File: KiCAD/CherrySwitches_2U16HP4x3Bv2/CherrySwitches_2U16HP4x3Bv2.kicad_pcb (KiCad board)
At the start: 2 copper layers, 80.9 x 84 mm, 16 parts

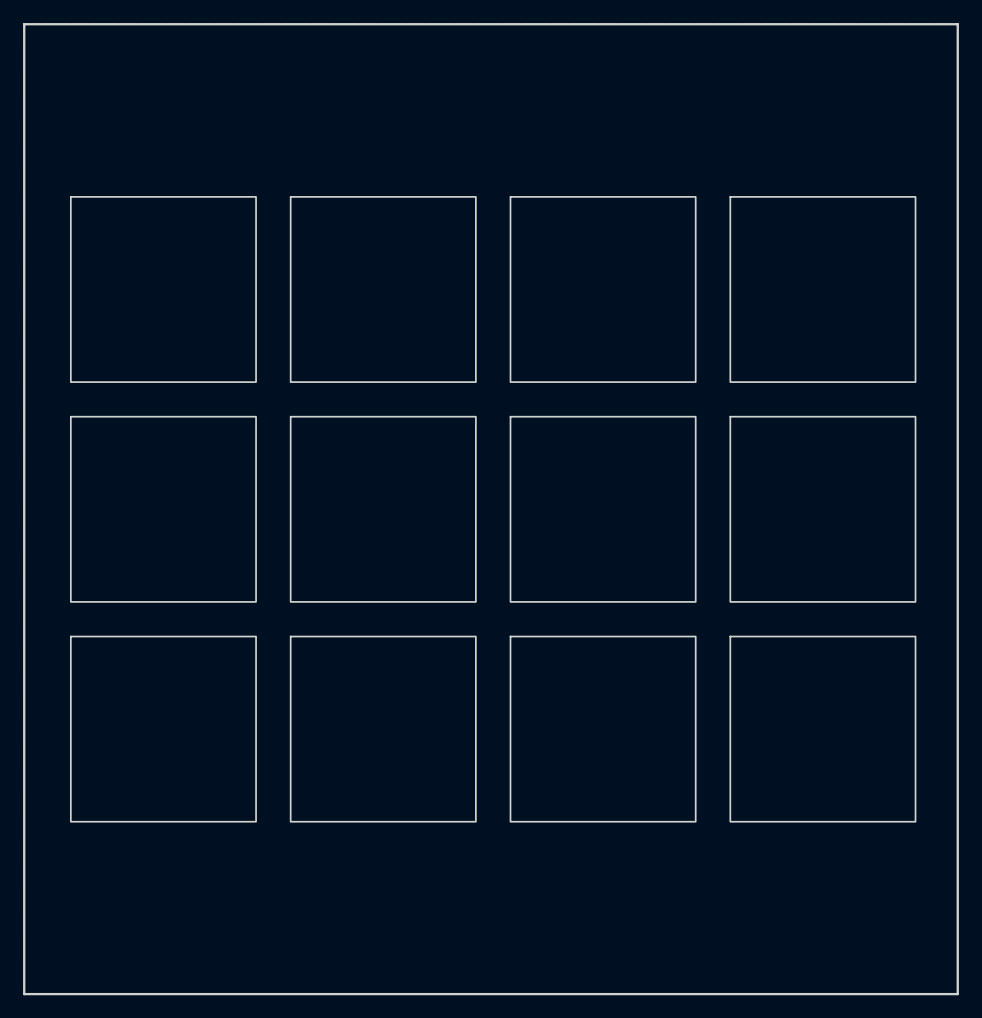
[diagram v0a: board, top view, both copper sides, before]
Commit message: updated all modules to use plated through-holes wherever possible
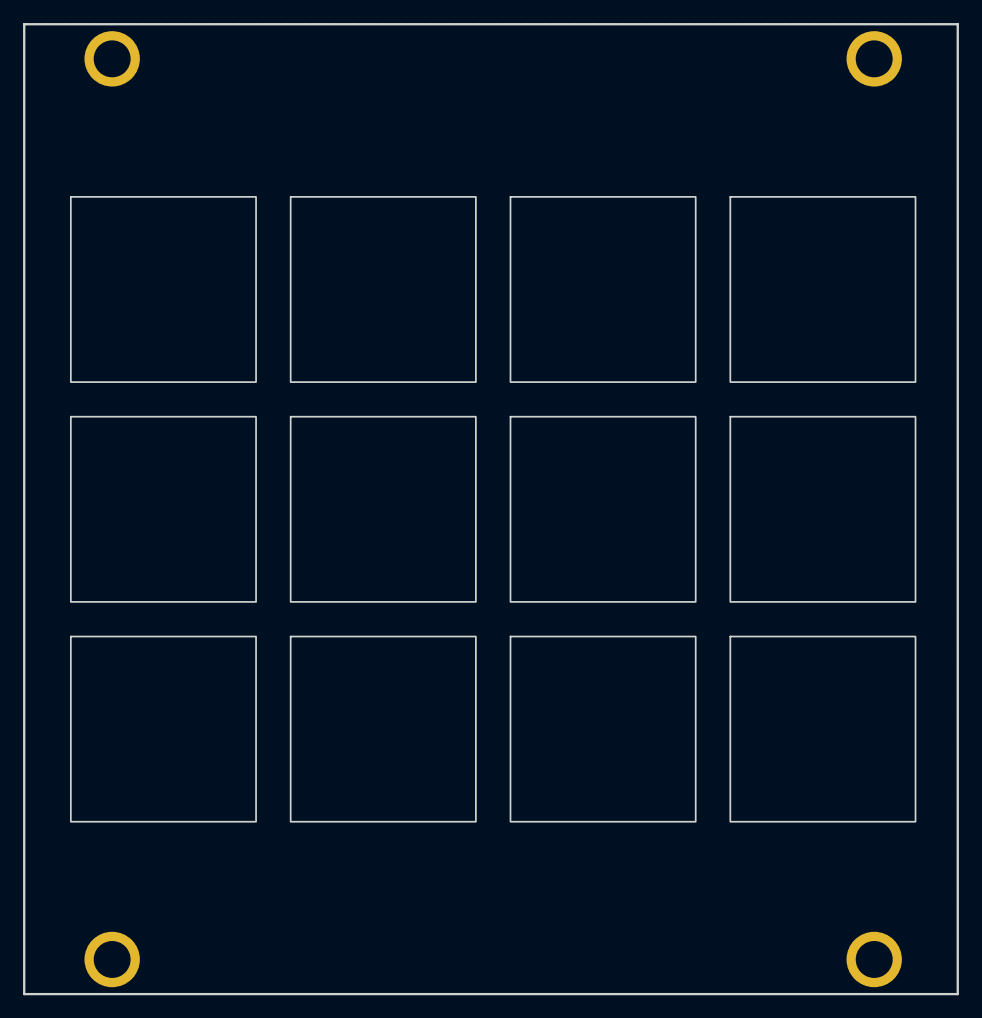
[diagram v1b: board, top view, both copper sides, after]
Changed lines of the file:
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@@
 			)
 		)
-		(pad "" np_thru_hole oval
+		(pad "" thru_hole circle
 			(at 0 0)
-			(size 4.34 3.2)
-			(drill oval 4.34 3.2)
+			(size 4.8 4.8)
+			(drill 3.2)
 			(layers "*.Cu" "*.Mask")
+			(remove_unused_layers no)
 		)
 		(embedded_fonts no)
@@
 			)
 		)
-		(pad "" np_thru_hole oval
+		(pad "" thru_hole circle
 			(at 0 0)
-			(size 4.34 3.2)
-			(drill oval 4.34 3.2)
+			(size 4.8 4.8)
+			(drill 3.2)
 			(layers "*.Cu" "*.Mask")
+			(remove_unused_layers no)
 		)
 		(embedded_fonts no)
@@
 			)
 		)
-		(pad "" np_thru_hole oval
+		(pad "" thru_hole circle
 			(at 0 0)
-			(size 4.34 3.2)
-			(drill oval 4.34 3.2)
+			(size 4.8 4.8)
+			(drill 3.2)
 			(layers "*.Cu" "*.Mask")
+			(remove_unused_layers no)
 		)
 		(embedded_fonts no)
@@
 			)
 		)
-		(pad "" np_thru_hole oval
+		(pad "" thru_hole circle
 			(at 0 0)
-			(size 4.34 3.2)
-			(drill oval 4.34 3.2)
+			(size 4.8 4.8)
+			(drill 3.2)
 			(layers "*.Cu" "*.Mask")
+			(remove_unused_layers no)
 		)
 		(embedded_fonts no)
